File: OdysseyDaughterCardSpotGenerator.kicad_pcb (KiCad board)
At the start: 2 copper layers, 47.8 x 46.6 mm, 1 part, among them X1 OdysseyDaughterCard

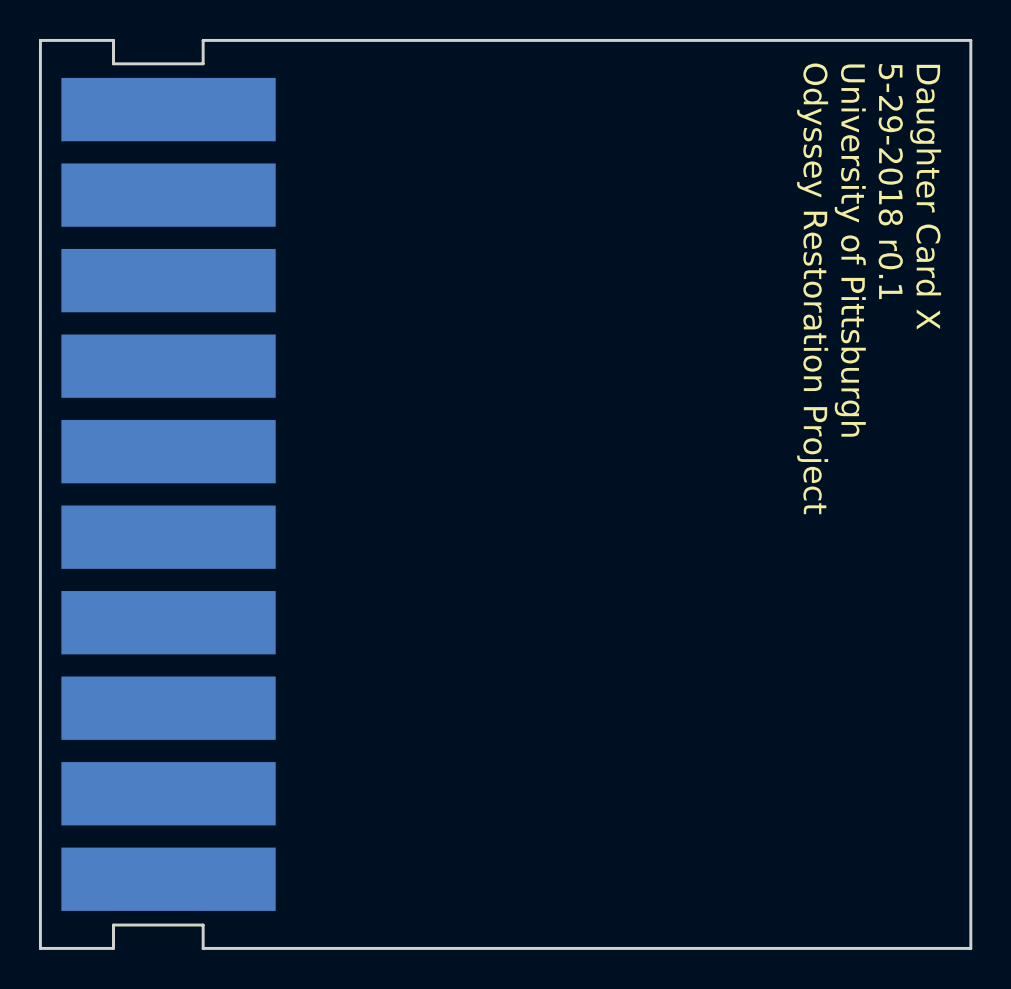
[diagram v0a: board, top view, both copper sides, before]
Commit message: Layout components on PCB
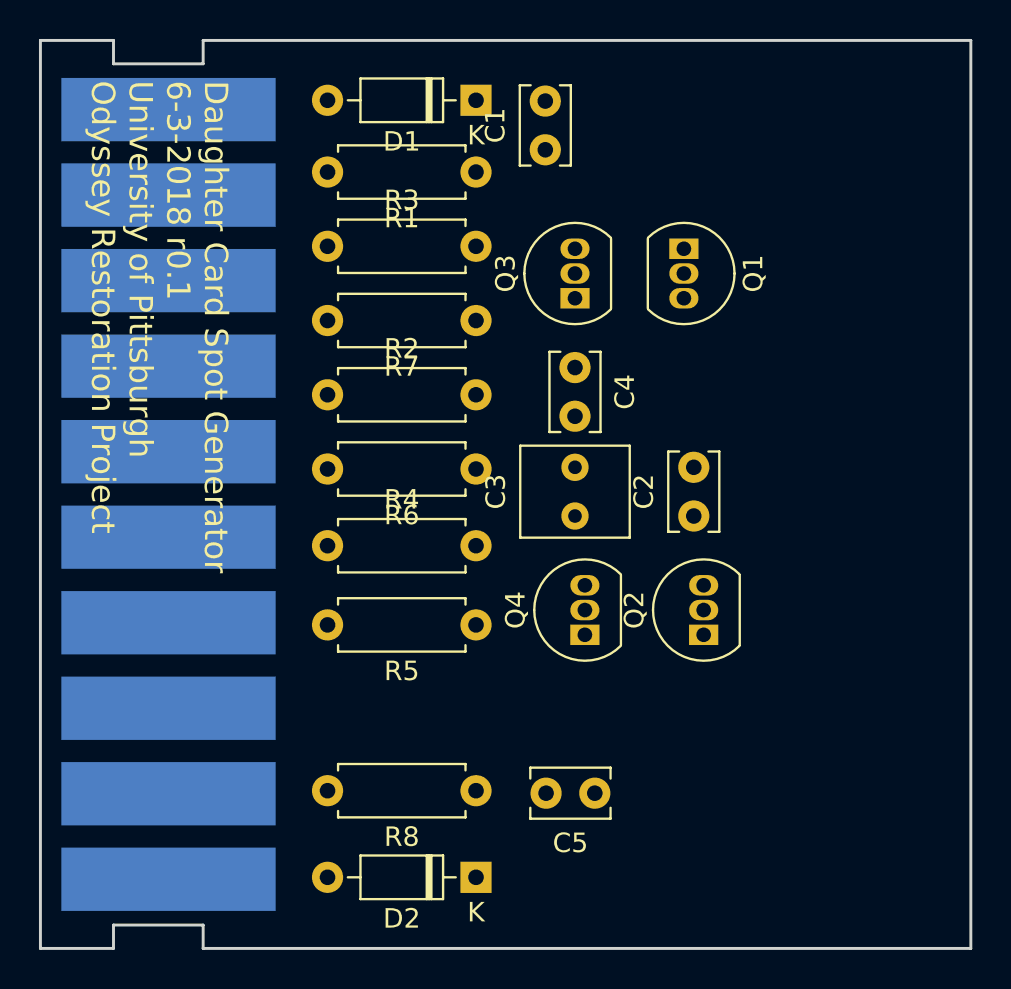
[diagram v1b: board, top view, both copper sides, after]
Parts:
- added C1: 1500p, Capacitor_THT:C_Rect_L4.0mm_W2.5mm_P2.50mm, F.Cu at (148.3, 83.3)
- added C2: 120p, Capacitor_THT:C_Rect_L4.0mm_W2.5mm_P2.50mm, F.Cu at (156.0, 102.1)
- added C3: 0.15u, Capacitor_THT:C_Rect_L4.6mm_W5.5mm_P2.50mm_MKS02_FKP02, F.Cu at (149.9, 102.1)
- added C4: 0.1u, Capacitor_THT:C_Rect_L4.0mm_W2.5mm_P2.50mm, F.Cu at (149.9, 94.5)
- added C5: 0.01u, Capacitor_THT:C_Rect_L4.0mm_W2.5mm_P2.50mm, F.Cu at (150.9, 116.3)
- added D1: 1N4448, Diode_THT:D_DO-35_SOD27_P7.62mm_Horizontal, F.Cu at (144.8, 80.8)
- added D2: 1N4448, Diode_THT:D_DO-35_SOD27_P7.62mm_Horizontal, F.Cu at (144.8, 120.7)
- added Q1: 2N3904, Package_TO_SOT_THT:TO-92_Inline, F.Cu at (155.4, 88.4)
- added Q2: 2N3904, Package_TO_SOT_THT:TO-92_Inline, F.Cu at (156.5, 108.2)
- added Q3: BC547C, Package_TO_SOT_THT:TO-92_Inline, F.Cu at (149.9, 90.9)
- added Q4: 2N3904, Package_TO_SOT_THT:TO-92_Inline, F.Cu at (150.4, 108.2)
- added R1: 10k, Resistor_THT:R_Axial_DIN0207_L6.3mm_D2.5mm_P7.62mm_Horizontal, F.Cu at (144.8, 84.5)
- added R2: 100K, Resistor_THT:R_Axial_DIN0207_L6.3mm_D2.5mm_P7.62mm_Horizontal, F.Cu at (137.2, 95.9)
- added R3: 10k, Resistor_THT:R_Axial_DIN0207_L6.3mm_D2.5mm_P7.62mm_Horizontal, F.Cu at (137.2, 88.3)
- added R4: 2.2k, Resistor_THT:R_Axial_DIN0207_L6.3mm_D2.5mm_P7.62mm_Horizontal, F.Cu at (137.2, 103.6)
- added R5: 10k, Resistor_THT:R_Axial_DIN0207_L6.3mm_D2.5mm_P7.62mm_Horizontal, F.Cu at (144.8, 107.7)
- added R6: 270K, Resistor_THT:R_Axial_DIN0207_L6.3mm_D2.5mm_P7.62mm_Horizontal, F.Cu at (144.8, 99.7)
- added R7: 10k, Resistor_THT:R_Axial_DIN0207_L6.3mm_D2.5mm_P7.62mm_Horizontal, F.Cu at (144.8, 92.1)
- added R8: 10k, Resistor_THT:R_Axial_DIN0207_L6.3mm_D2.5mm_P7.62mm_Horizontal, F.Cu at (144.8, 116.2)
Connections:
- X1 pad 1: Net-(X1-Pad1) -> /Card1
- X1 pad 10: Net-(X1-Pad10) -> /Card10
- X1 pad 2: Net-(X1-Pad2) -> /Card2
- X1 pad 3: Net-(X1-Pad3) -> GND
- X1 pad 4: Net-(X1-Pad4) -> /Card4
- X1 pad 5: Net-(X1-Pad5) -> /Card5
- X1 pad 6: Net-(X1-Pad6) -> /Card6
- X1 pad 7: Net-(X1-Pad7) -> /Card7
- X1 pad 8: Net-(X1-Pad8) -> /Card8
- X1 pad 9: Net-(X1-Pad9) -> /Card9
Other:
- board text added: "Daughter Card Spot Generator 6-3-2018 r0.1 University of Pittsburgh Odyssey Restoration Project"
- board text removed: "Daughter Card X 5-29-2018 r0.1 University of Pittsburgh Odyssey Restoration Project"

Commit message: Use autorouter
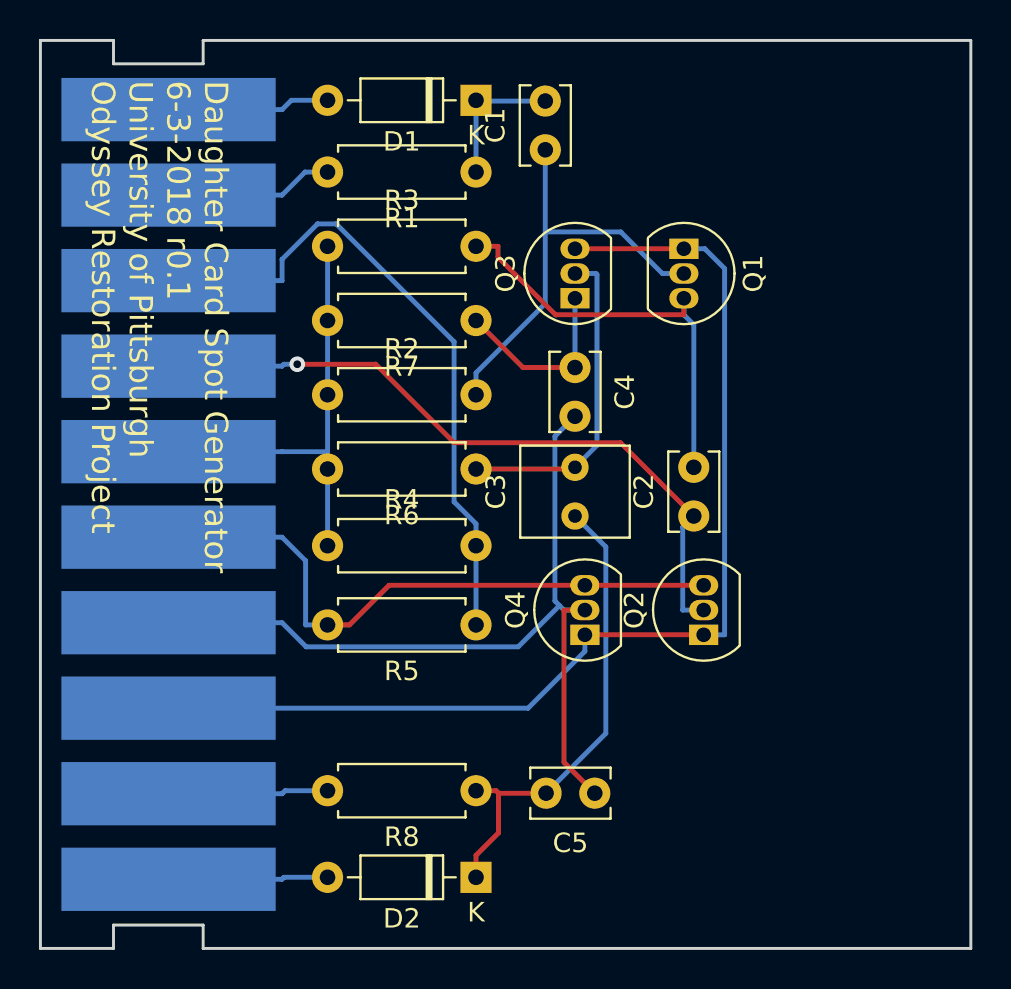
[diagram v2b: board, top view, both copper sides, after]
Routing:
- net GND: track 0.00 -> 57.5 mm
- net /Card4: track 0.00 -> 44.2 mm
- net /Card7: track 0.00 -> 36.4 mm, vias 0 -> 1
- net /Card8: track 0.00 -> 34.0 mm
- net /Card5: track 0.00 -> 32.1 mm
- net Net-(C3-Pad1): track 0.00 -> 24.6 mm
- net /Card6: track 0.00 -> 23.5 mm
- net Net-(C2-Pad2): track 0.00 -> 22.2 mm
- net Net-(C1-Pad1): track 0.00 -> 22.0 mm
- net Net-(C3-Pad2): track 0.00 -> 16.6 mm
- net Net-(C4-Pad1): track 0.00 -> 9.64 mm
- net /Card9: track 0.00 -> 8.65 mm
- net /Card10: track 0.00 -> 8.36 mm
- net /Card2: track 0.00 -> 8.22 mm
- net /Card1: track 0.00 -> 8.20 mm
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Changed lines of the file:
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@@
     (thickness 1.6)
     (drawings 13)
-    (tracks 0)
+    (tracks 104)
     (zones 0)
     (modules 20)
@@
   )
   (gr_line (start 122.425 124.3) (end 122.425 77.7) (layer Edge.Cuts) (width 0.15))
+  (segment (start 144.78 95.885) (end 144.78 94.7597) (width 0.25) (layer B.Cu) (net 1))
+  (segment (start 152.2116 87.5301) (end 148.336 87.5301) (width 0.25) (layer B.Cu) (net 1))
+  (segment (start 154.3435 89.662) (end 152.2116 87.5301) (width 0.25) (layer B.Cu) (net 1))
+  (segment (start 155.448 89.662) (end 154.3435 89.662) (width 0.25) (layer B.Cu) (net 1))
+  (segment (start 148.336 91.2037) (end 148.336 87.5301) (width 0.25) (layer B.Cu) (net 1))
+  (segment (start 144.78 94.7597) (end 148.336 91.2037) (width 0.25) (layer B.Cu) (net 1))
+  (segment (start 148.336 87.5301) (end 148.336 83.312) (width 0.25) (layer B.Cu) (net 1))
+  (segment (start 144.78 80.812) (end 148.336 80.812) (width 0.25) (layer B.Cu) (net 2))
+  (segment (start 144.78 84.455) (end 144.78 80.812) (width 0.25) (layer B.Cu) (net 2))
+  (segment (start 144.78 80.812) (end 144.78 80.772) (width 0.25) (layer B.Cu) (net 2))
+  (segment (start 148.8599 91.7823) (end 155.448 91.7823) (width 0.25) (layer F.Cu) (net 3))
+  (segment (start 145.9053 88.8277) (end 148.8599 91.7823) (width 0.25) (layer F.Cu) (net 3))
+  (segment (start 145.9053 88.265) (end 145.9053 88.8277) (width 0.25) (layer F.Cu) (net 3))
+  (segment (start 144.78 88.265) (end 145.9053 88.265) (width 0.25) (layer F.Cu) (net 3))
+  (segment (start 155.448 90.932) (end 155.448 91.7823) (width 0.25) (layer F.Cu) (net 3))
+  (segment (start 155.956 92.2903) (end 155.956 99.608) (width 0.25) (layer B.Cu) (net 3))
+  (segment (start 155.448 91.7823) (end 155.956 92.2903) (width 0.25) (layer B.Cu) (net 3))
+  (segment (start 155.448 90.932) (end 155.448 91.7823) (width 0.25) (layer B.Cu) (net 3))
+  (via (at 135.6058 94.3183) (size 0.8) (layers F.Cu B.Cu) (net 4))
+  (segment (start 156.464 106.934) (end 155.3887 106.934) (width 0.25) (layer B.Cu) (net 4))
+  (segment (start 155.3887 102.6753) (end 155.956 102.108) (width 0.25) (layer B.Cu) (net 4))
+  (segment (start 155.3887 106.934) (end 155.3887 102.6753) (width 0.25) (layer B.Cu) (net 4))
+  (segment (start 139.6338 94.3183) (end 135.6058 94.3183) (width 0.25) (layer F.Cu) (net 4))
+  (segment (start 143.6635 98.348) (end 139.6338 94.3183) (width 0.25) (layer F.Cu) (net 4))
+  (segment (start 152.196 98.348) (end 143.6635 98.348) (width 0.25) (layer F.Cu) (net 4))
+  (segment (start 155.956 102.108) (end 152.196 98.348) (width 0.25) (layer F.Cu) (net 4))
+  (segment (start 134.9237 94.3183) (end 134.8253 94.4167) (width 0.25) (layer B.Cu) (net 4))
+  (segment (start 135.6058 94.3183) (end 134.9237 94.3183) (width 0.25) (layer B.Cu) (net 4))
+  (segment (start 129 94.4167) (end 134.8253 94.4167) (width 0.25) (layer B.Cu) (net 4))
+  (segment (start 151.4434 113.2646) (end 148.376 116.332) (width 0.25) (layer B.Cu) (net 5))
+  (segment (start 151.4434 103.6914) (end 151.4434 113.2646) (width 0.25) (layer B.Cu) (net 5))
+  (segment (start 149.86 102.108) (end 151.4434 103.6914) (width 0.25) (layer B.Cu) (net 5))
+  (segment (start 145.9369 116.332) (end 148.376 116.332) (width 0.25) (layer F.Cu) (net 5))
+  (segment (start 145.8099 116.205) (end 145.9369 116.332) (width 0.25) (layer F.Cu) (net 5))
+  (segment (start 144.78 116.205) (end 145.8099 116.205) (width 0.25) (layer F.Cu) (net 5))
+  (segment (start 145.9369 118.3678) (end 144.78 119.5247) (width 0.25) (layer F.Cu) (net 5))
+  (segment (start 145.9369 116.332) (end 145.9369 118.3678) (width 0.25) (layer F.Cu) (net 5))
+  (segment (start 144.78 120.65) (end 144.78 119.5247) (width 0.25) (layer F.Cu) (net 5))
+  (segment (start 150.9893 98.4787) (end 149.86 99.608) (width 0.25) (layer B.Cu) (net 6))
+  (segment (start 150.9893 89.716) (end 150.9893 98.4787) (width 0.25) (layer B.Cu) (net 6))
+  (segment (start 150.9353 89.662) (end 150.9893 89.716) (width 0.25) (layer B.Cu) (net 6))
+  (segment (start 149.86 89.662) (end 150.9353 89.662) (width 0.25) (layer B.Cu) (net 6))
+  (segment (start 149.773 99.695) (end 149.86 99.608) (width 0.25) (layer F.Cu) (net 6))
+  (segment (start 144.78 99.695) (end 149.773 99.695) (width 0.25) (layer F.Cu) (net 6))
+  (segment (start 147.193 94.488) (end 149.86 94.488) (width 0.25) (layer F.Cu) (net 7))
+  (segment (start 144.78 92.075) (end 147.193 94.488) (width 0.25) (layer F.Cu) (net 7))
+  (segment (start 149.86 90.932) (end 149.86 94.488) (width 0.25) (layer B.Cu) (net 7))
+  (segment (start 149.2927 114.7487) (end 149.2927 106.934) (width 0.25) (layer F.Cu) (net 8))
+  (segment (start 150.876 116.332) (end 149.2927 114.7487) (width 0.25) (layer F.Cu) (net 8))
+  (segment (start 150.368 106.934) (end 149.2927 106.934) (width 0.25) (layer F.Cu) (net 8))
+  (segment (start 150.368 106.934) (end 149.2927 106.934) (width 0.25) (layer B.Cu) (net 8))
+  (segment (start 149.2927 106.934) (end 149.0625 106.7037) (width 0.25) (layer B.Cu) (net 8))
+  (segment (start 136.0634 108.8214) (end 134.8253 107.5833) (width 0.25) (layer B.Cu) (net 8))
+  (segment (start 146.9448 108.8214) (end 136.0634 108.8214) (width 0.25) (layer B.Cu) (net 8))
+  (segment (start 149.0625 106.7037) (end 146.9448 108.8214) (width 0.25) (layer B.Cu) (net 8))
+  (segment (start 129 107.5833) (end 134.8253 107.5833) (width 0.25) (layer B.Cu) (net 8))
+  (segment (start 148.8322 98.0158) (end 149.86 96.988) (width 0.25) (layer B.Cu) (net 8))
+  (segment (start 148.8322 106.4734) (end 148.8322 98.0158) (width 0.25) (layer B.Cu) (net 8))
+  (segment (start 149.0625 106.7037) (end 148.8322 106.4734) (width 0.25) (layer B.Cu) (net 8))
+  (segment (start 135.3033 80.772) (end 134.8253 81.25) (width 0.25) (layer B.Cu) (net 9))
+  (segment (start 137.16 80.772) (end 135.3033 80.772) (width 0.25) (layer B.Cu) (net 9))
+  (segment (start 129 81.25) (end 134.8253 81.25) (width 0.25) (layer B.Cu) (net 9))
+  (segment (start 134.9253 120.65) (end 134.8253 120.75) (width 0.25) (layer B.Cu) (net 10))
+  (segment (start 137.16 120.65) (end 134.9253 120.65) (width 0.25) (layer B.Cu) (net 10))
+  (segment (start 129 120.75) (end 134.8253 120.75) (width 0.25) (layer B.Cu) (net 10))
+  (segment (start 149.86 88.392) (end 155.448 88.392) (width 0.25) (layer F.Cu) (net 11))
+  (segment (start 156.464 108.204) (end 150.368 108.204) (width 0.25) (layer F.Cu) (net 11))
+  (segment (start 157.5393 89.408) (end 156.5233 88.392) (width 0.25) (layer B.Cu) (net 11))
+  (segment (start 157.5393 108.204) (end 157.5393 89.408) (width 0.25) (layer B.Cu) (net 11))
+  (segment (start 156.464 108.204) (end 157.5393 108.204) (width 0.25) (layer B.Cu) (net 11))
+  (segment (start 155.448 88.392) (end 156.5233 88.392) (width 0.25) (layer B.Cu) (net 11))
+  (segment (start 147.4501 111.9722) (end 129 111.9722) (width 0.25) (layer B.Cu) (net 11))
+  (segment (start 150.368 109.0543) (end 147.4501 111.9722) (width 0.25) (layer B.Cu) (net 11))
+  (segment (start 150.368 108.204) (end 150.368 109.0543) (width 0.25) (layer B.Cu) (net 11))
+  (segment (start 156.464 105.664) (end 150.368 105.664) (width 0.25) (layer F.Cu) (net 12))
+  (segment (start 136.0347 104.4038) (end 134.8253 103.1944) (width 0.25) (layer B.Cu) (net 12))
+  (segment (start 136.0347 107.696) (end 136.0347 104.4038) (width 0.25) (layer B.Cu) (net 12))
+  (segment (start 137.16 107.696) (end 136.0347 107.696) (width 0.25) (layer B.Cu) (net 12))
+  (segment (start 129 103.1944) (end 134.8253 103.1944) (width 0.25) (layer B.Cu) (net 12))
+  (segment (start 140.3173 105.664) (end 150.368 105.664) (width 0.25) (layer F.Cu) (net 12))
+  (segment (start 138.2853 107.696) (end 140.3173 105.664) (width 0.25) (layer F.Cu) (net 12))
+  (segment (start 137.16 107.696) (end 138.2853 107.696) (width 0.25) (layer F.Cu) (net 12))
+  (segment (start 136.0092 84.455) (end 134.8253 85.6389) (width 0.25) (layer B.Cu) (net 13))
+  (segment (start 137.16 84.455) (end 136.0092 84.455) (width 0.25) (layer B.Cu) (net 13))
+  (segment (start 129 85.6389) (end 134.8253 85.6389) (width 0.25) (layer B.Cu) (net 13))
+  (segment (start 137.16 88.265) (end 137.16 92.075) (width 0.25) (layer B.Cu) (net 14))
+  (segment (start 137.16 92.075) (end 137.16 95.885) (width 0.25) (layer B.Cu) (net 14))
+  (segment (start 137.16 99.695) (end 137.16 103.632) (width 0.25) (layer B.Cu) (net 14))
+  (segment (start 129 98.8055) (end 134.8253 98.8055) (width 0.25) (layer B.Cu) (net 14))
+  (segment (start 137.16 98.8055) (end 134.8253 98.8055) (width 0.25) (layer B.Cu) (net 14))
+  (segment (start 137.16 95.885) (end 137.16 98.8055) (width 0.25) (layer B.Cu) (net 14))
+  (segment (start 137.16 98.8055) (end 137.16 99.695) (width 0.25) (layer B.Cu) (net 14))
+  (segment (start 144.78 107.696) (end 144.78 103.632) (width 0.25) (layer B.Cu) (net 15))
+  (segment (start 143.6547 101.3814) (end 144.78 102.5067) (width 0.25) (layer B.Cu) (net 15))
+  (segment (start 143.6547 93.1645) (end 143.6547 101.3814) (width 0.25) (layer B.Cu) (net 15))
+  (segment (start 137.6055 87.1153) (end 143.6547 93.1645) (width 0.25) (layer B.Cu) (net 15))
+  (segment (start 136.6457 87.1153) (end 137.6055 87.1153) (width 0.25) (layer B.Cu) (net 15))
+  (segment (start 134.8253 88.9357) (end 136.6457 87.1153) (width 0.25) (layer B.Cu) (net 15))
+  (segment (start 134.8253 90.0278) (end 134.8253 88.9357) (width 0.25) (layer B.Cu) (net 15))
+  (segment (start 129 90.0278) (end 134.8253 90.0278) (width 0.25) (layer B.Cu) (net 15))
+  (segment (start 144.78 103.632) (end 144.78 102.5067) (width 0.25) (layer B.Cu) (net 15))
+  (segment (start 134.9814 116.205) (end 134.8253 116.3611) (width 0.25) (layer B.Cu) (net 16))
+  (segment (start 137.16 116.205) (end 134.9814 116.205) (width 0.25) (layer B.Cu) (net 16))
+  (segment (start 129 116.3611) (end 134.8253 116.3611) (width 0.25) (layer B.Cu) (net 16))
 )

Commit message: Fix PCB component annotations
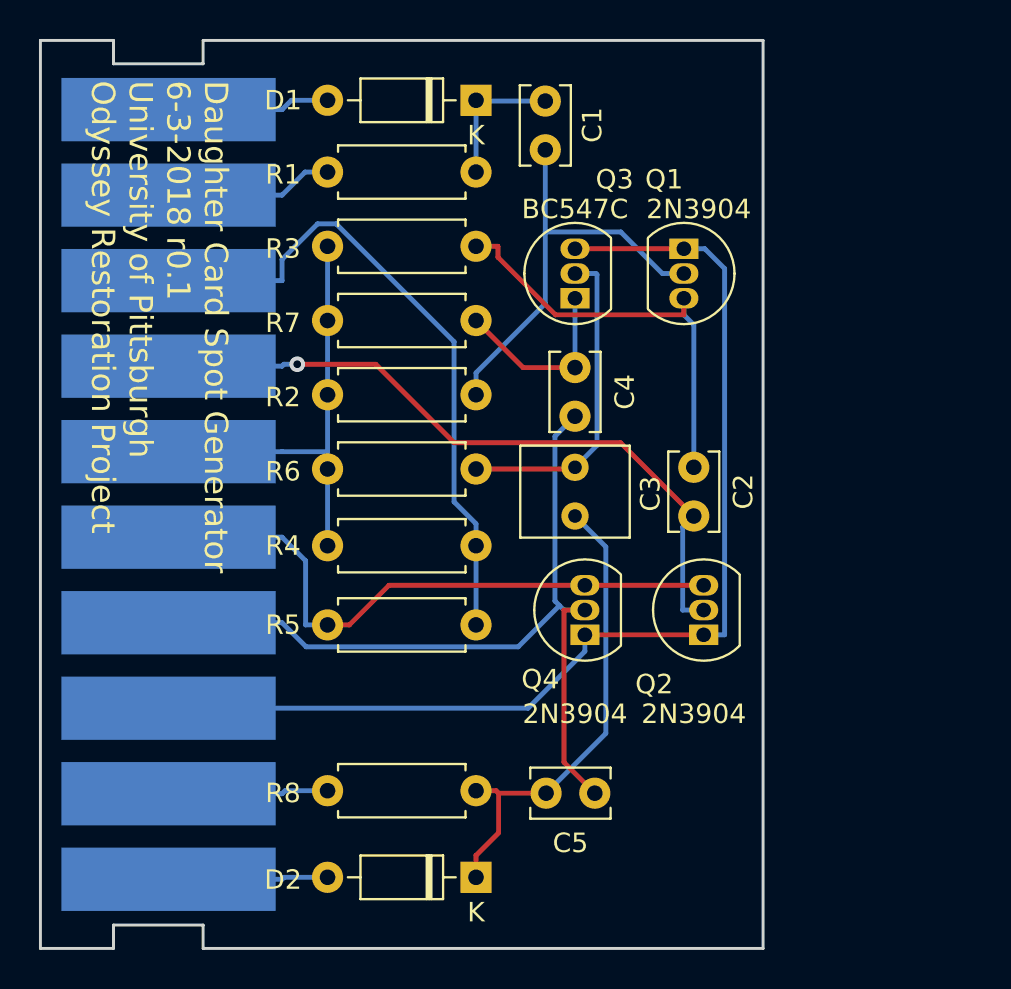
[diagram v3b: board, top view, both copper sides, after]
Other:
- board size 47.8 x 46.6 mm -> 37.1 x 46.6 mm
